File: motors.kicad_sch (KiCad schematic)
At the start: 13 parts, among them M1 Motor_DC, M2 Motor_DC, M3 Stepper_Motor_bipolar, M4 Motor_Servo_Hitec, M5 Motor_DC, Q2 NMOS, Q3 NPN, U4 L293D, U5 L293D

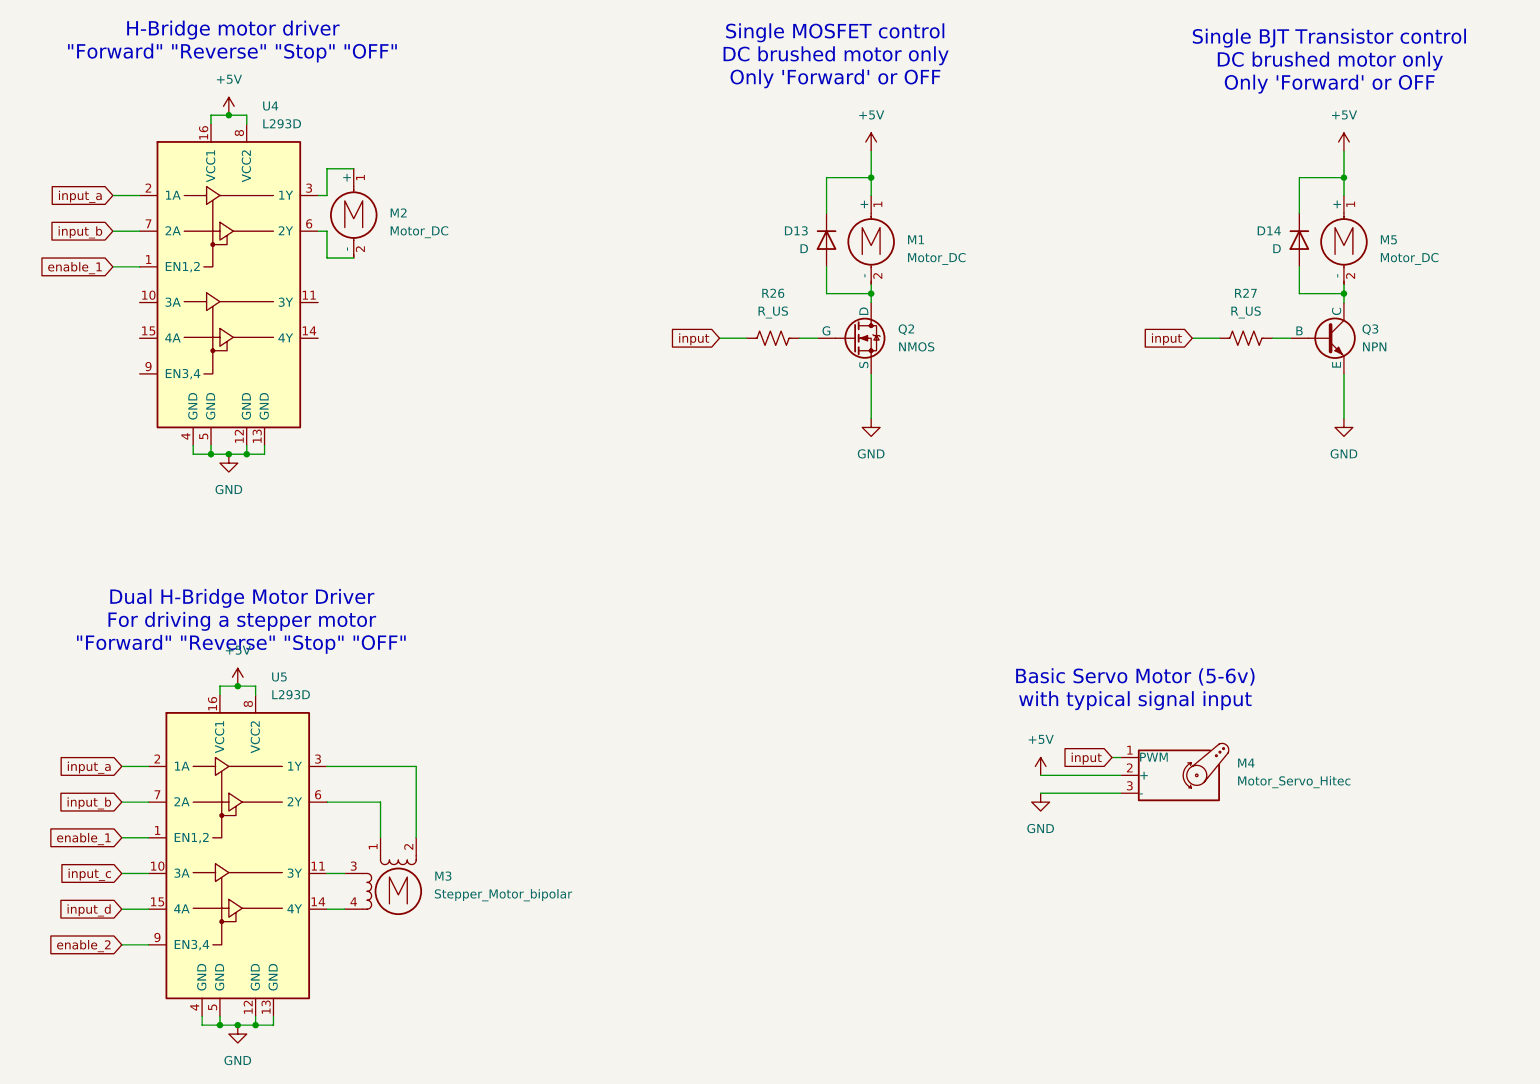
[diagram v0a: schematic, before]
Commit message: new pages added
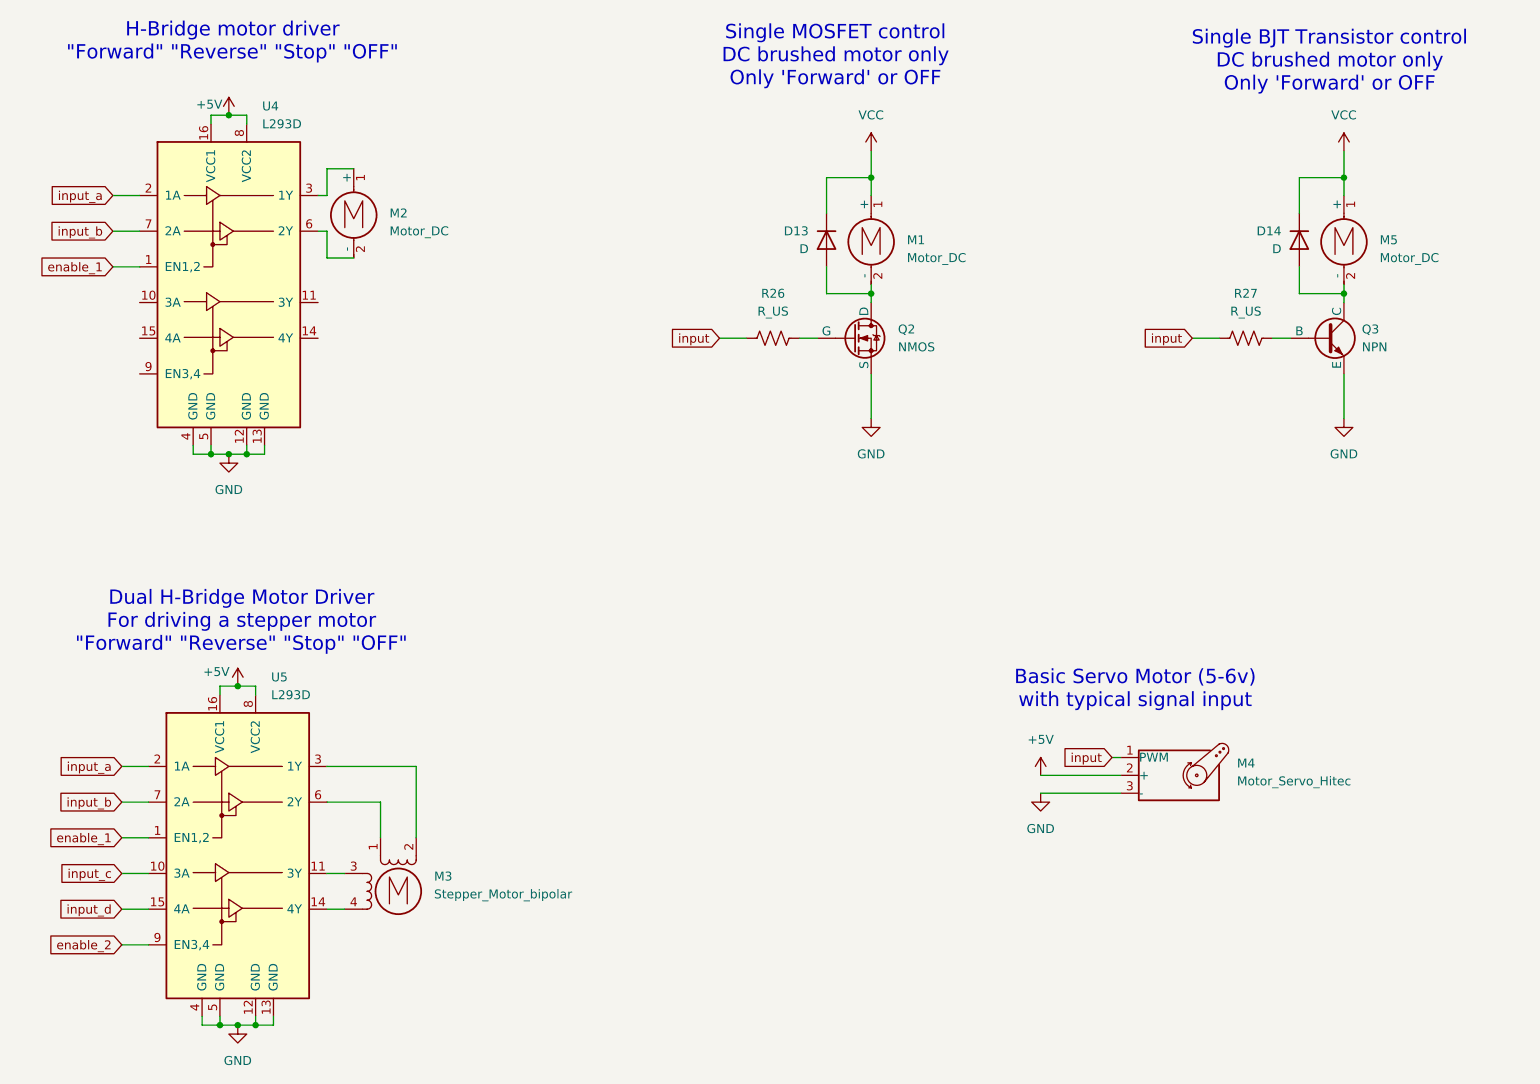
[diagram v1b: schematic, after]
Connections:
- net +5V: no longer D13.1 (K), D14.1 (K), M1.1 (+), M5.1 (+)
- new net VCC: D13.1 (K), D14.1 (K), M1.1 (+), M5.1 (+)
